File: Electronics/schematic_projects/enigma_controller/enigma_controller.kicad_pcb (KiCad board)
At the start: 6 copper layers, 142.6 x 120.8 mm, 89 parts, among them IC1 TPD8S300ARUKR, IC10 MCP23017-E_SO, IC11 RT9742SNGV, IC13 ESD224DQAR, IC14 ESD224DQAR, IC2 ESD321DYAR, IC3 ESD321DYAR, IC4 ESD321DYAR, IC5 ESD321DYAR, IC6 ESD321DYAR, IC7 ESD321DYAR, IC8 AP22653W6-7, IC9 MCP23017-E_SO, J1 Conn_02x05_Odd_Even, J10 A70-112-331N126, J11 Conn_02x05_Odd_Even, J12 Conn_01x02, J15 Conn_01x02, J16 Conn_01x02, J17 Conn_01x02, J18 Conn_01x02, J19 Conn_01x02, J2 Conn_02x04_Odd_Even, J20 Conn_01x02, J21 Conn_02x05_Odd_Even, J22 Conn_02x05_Odd_Even, J23 Conn_01x02, J24 Conn_01x02, J25 Conn_01x02, J26 Conn_01x02, J27 Conn_01x02, J3 USB1040-GF-L-B, J4 USB_C_Receptacle_USB2.0_16P, J5 HDMI_A_1.4, J6 Conn_02x05_Odd_Even, J7 Conn_02x07_Odd_Even, J8 USB3_A_Stacked, J9 Conn_02x07_Odd_Even, M1 Fan_4pin

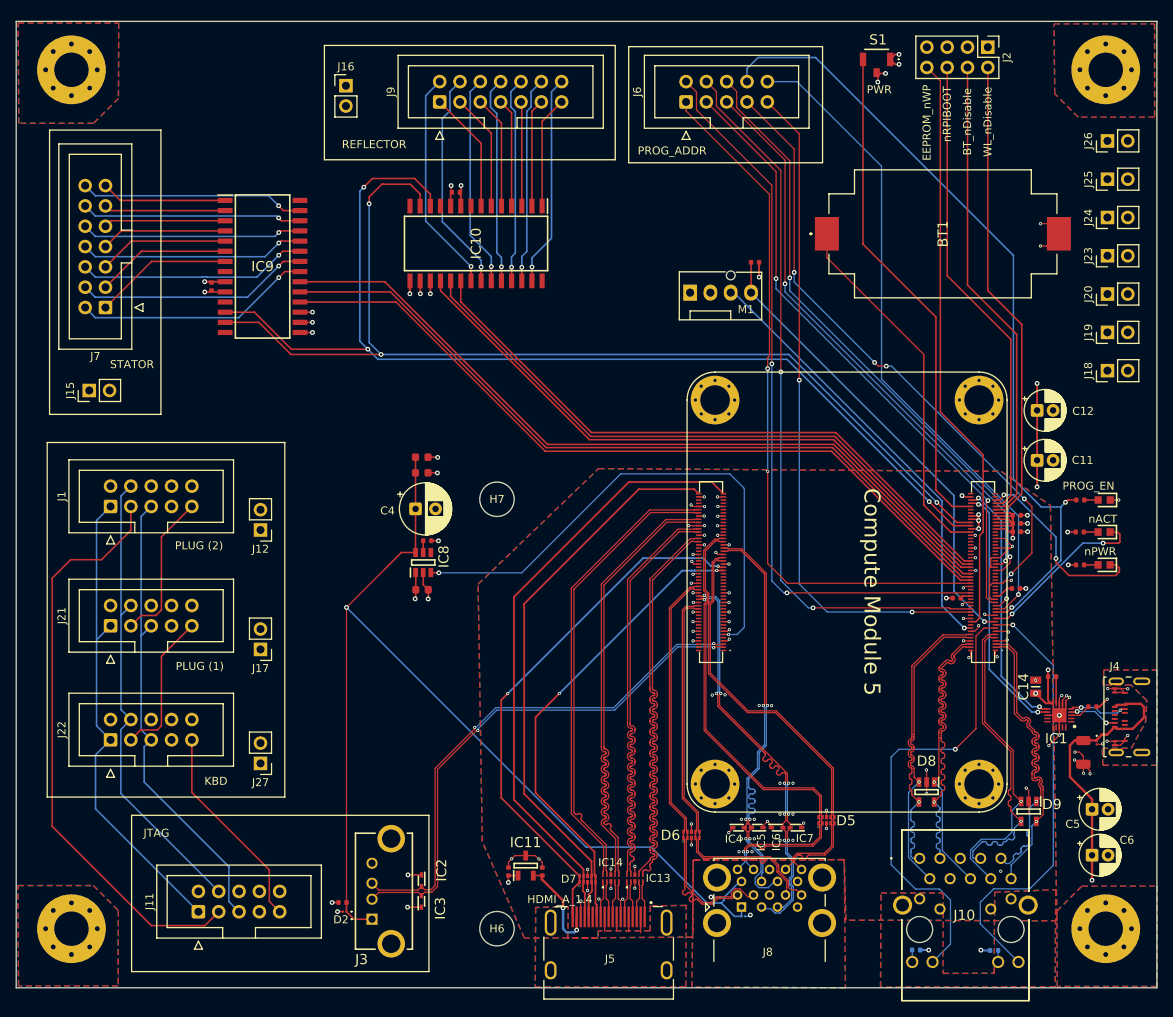
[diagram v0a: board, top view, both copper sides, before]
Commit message: Updated with board-2-board connectors.
Also re-organised components to reduce PCB size.
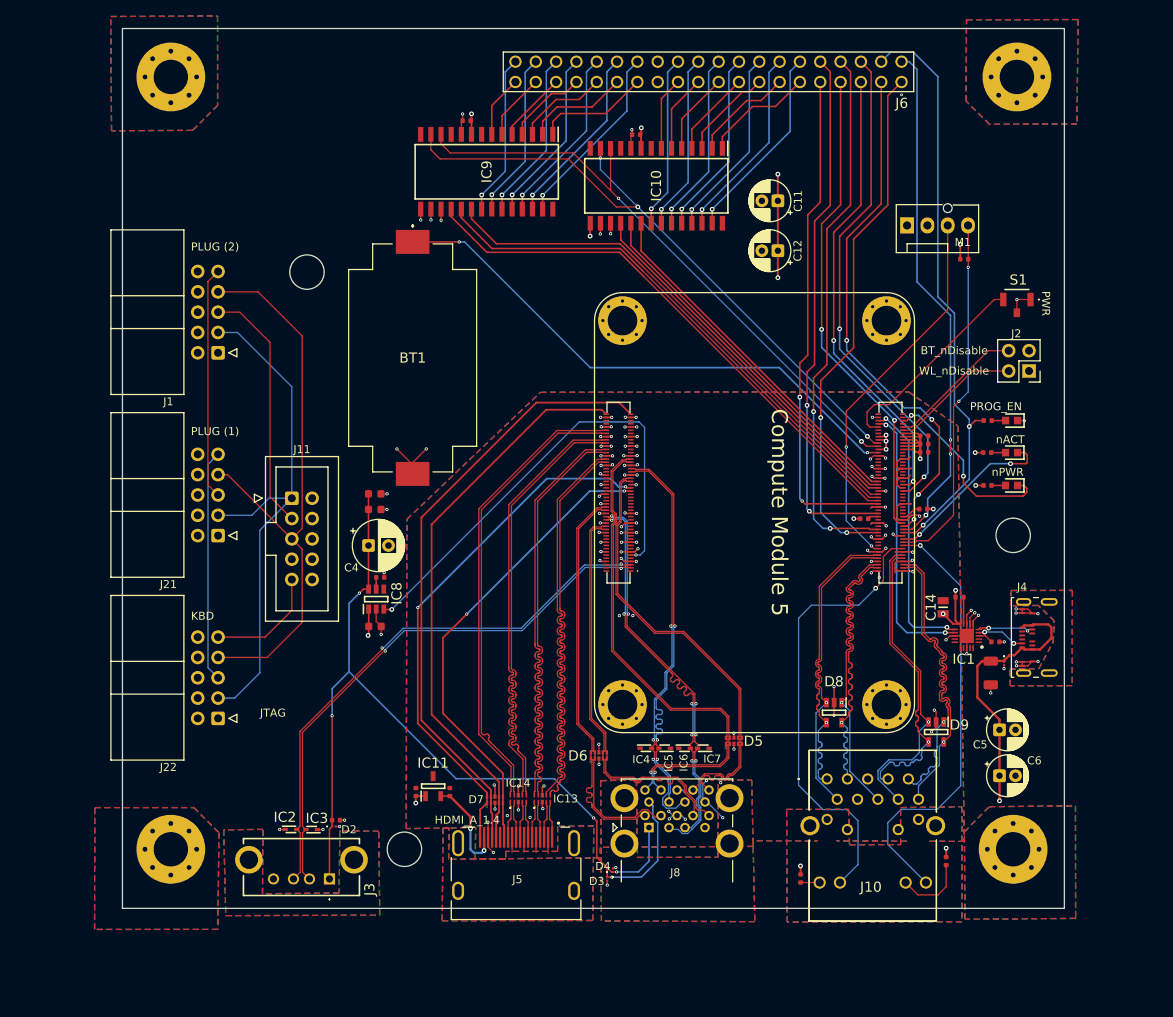
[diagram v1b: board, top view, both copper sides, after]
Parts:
- removed J12, J15, J16, J17, J18, J19, J20, J23, J24, J25, J26, J27: Conn_01x02, Connector_PinHeader_2.54mm:PinHeader_1x02_P2.54mm_Vertical
- removed J7, J9: Conn_02x07_Odd_Even, Connector_IDC:IDC-Header_2x07_P2.54mm_Vertical
- added H8: MountingHole, MountingHole:MountingHole_4.3mm_M4, F.Cu at (193.5, 97.1)
- D3, D4, R3, R4: moved to F.Cu
- J1, J21, J22: footprint Connector_IDC:IDC-Header_2x05_P2.54mm_Vertical -> Connector_IDC:IDC-Header_2x05_P2.54mm_Horizontal
- J2: value Conn_02x04_Odd_Even -> Conn_02x02_Odd_Even; footprint Connector_PinHeader_2.54mm:PinHeader_2x04_P2.54mm_Vertical -> Connector_PinHeader_2.54mm:PinHeader_2x02_P2.54mm_Vertical
- J6: value Conn_02x05_Odd_Even -> ESW-120-33-G-D; footprint Connector_IDC:IDC-Header_2x05_P2.54mm_Vertical -> Enigma_Components:ESW-120-XX-Y-D
- moved BT1 68.1 mm to (118.5, 75.0), turned to 0 degrees
- moved J11 53.0 mm to (103.3, 92.5), turned to 0 degrees
- moved C11 45.9 mm to (164.1, 55.3), turned to 180 degrees
- moved J2 40.8 mm to (195.5, 76.6), turned to 180 degrees
- moved C12 38.1 mm to (164.1, 61.6), turned to 180 degrees
- moved C20 38.0 mm to (125.2, 45.3), turned to 180 degrees
- moved H7 37.0 mm to (105.2, 64.2)
- moved S1 34.8 mm to (194.0, 67.7)
- moved IC9 30.4 mm to (127.7, 51.7), turned to -90 degrees
- moved M1 28.4 mm to (180.3, 58.4)
- moved J6 27.0 mm to (179.6, 40.5), turned to 0 degrees
- moved R8 26.2 mm to (187.4, 62.6), turned to 0 degrees
- moved C17 23.7 mm to (146.4, 47.0)
- moved IC10 23.7 mm to (148.9, 53.4)
- moved J1 23.4 mm to (94.1, 74.3), turned to 180 degrees
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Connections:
- H1 pad 20: /EEPROM_nWP -> unconnected-(H1A-EEPROM_nWP-Pad20)
- H1 pad 93: /nRPIBOOT -> unconnected-(H1A-nRPIBOOT-Pad93)
- J1 pad 1: /TCK -> /VCC_JTAG
- J1 pad 3: /TDO -> /TCK
- J1 pad 4: /VCC_JTAG -> GND
- J1 pad 5: /TMS -> /TDO
- J1 pad 6: unconnected-(J1-Pin_6-Pad6) -> GND
- J1 pad 7: unconnected-(J1-Pin_7-Pad7) -> /TMS
- J1 pad 8: unconnected-(J1-Pin_8-Pad8) -> GND
- J21 pad 1: /TCK -> /VCC_JTAG
- J21 pad 3: /TDX2 -> /TCK
- J21 pad 4: /VCC_JTAG -> GND
- J21 pad 5: /TMS -> /TDX2
- J21 pad 6: unconnected-(J21-Pin_6-Pad6) -> GND
- J21 pad 7: unconnected-(J21-Pin_7-Pad7) -> /TMS
- J21 pad 8: unconnected-(J21-Pin_8-Pad8) -> GND
- J22 pad 1: /TCK -> /VCC_JTAG
- J22 pad 3: /TDX1 -> /TCK
- J22 pad 4: /VCC_JTAG -> GND
- J22 pad 5: /TMS -> /TDX1
- J22 pad 6: unconnected-(J22-Pin_6-Pad6) -> GND
- J22 pad 7: unconnected-(J22-Pin_7-Pad7) -> /TMS
- J22 pad 8: unconnected-(J22-Pin_8-Pad8) -> GND
- J6 pad 1: /MAP_ADDR_1 -> /PROG_nWE_A
- J6 pad 10: /PROG_nWE_B -> /MAP_ADDR_2
- J6 pad 2: /MAP_ADDR_2 -> /PROG_nWE_B
- J6 pad 3: /MAP_ADDR_3 -> /MAP_ADDR_7
- J6 pad 4: /MAP_ADDR_4 -> /PROG_EN
- J6 pad 7: /MAP_ADDR_7 -> /MAP_ADDR_3
- J6 pad 8: /PROG_EN -> /MAP_ADDR_4
- J6 pad 9: /PROG_nWE_A -> /MAP_ADDR_1
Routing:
- net /EEPROM_nWP: track 73.2 -> 0.00 mm
- net /I2C_SCL: track 136.2 -> 76.7 mm, vias 3 -> 2
- net /nRPIBOOT: track 59.1 -> 0.00 mm
- net /VCC_JTAG: track 59.0 -> 0.00 mm
- net /I2C_SDA: track 132.9 -> 82.3 mm
- net /WL_nDisable: track 59.2 -> 16.3 mm
- net /BT_nDisable: track 59.2 -> 17.2 mm
- net /TDO: track 73.0 -> 31.2 mm
- net Net-(H1A-PWR_Button): track 62.8 -> 25.9 mm
- net /EXP2_INT_A: track 79.8 -> 45.0 mm
- net /EXP2_nRST: track 81.8 -> 47.1 mm
- net /EXP2_INT_B: track 80.8 -> 46.1 mm
- net /EXP1_INT_A: track 99.0 -> 66.3 mm
- net /EXP1_INT_B: track 98.6 -> 67.7 mm
- net /EXP1_nRST: track 98.2 -> 69.0 mm
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- added copper zone on In3.Cu, net /VCC_JTAG
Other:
- board size 142.6 x 120.8 mm -> 117.7 x 110 mm
- board text removed: "EEPROM_nWP"
- board text removed: "PROG_ADDR"
- board text removed: "REFLECTOR"
- board text removed: "STATOR"
- board text removed: "nRPIBOOT"

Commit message: Slight re-organisation of USB current limiter.
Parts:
- moved C18 21.6 mm to (114.6, 130.1)
- moved C19 21.6 mm to (114.6, 115.5)
- moved C3 21.6 mm to (114.6, 113.5)
- moved R9 21.6 mm to (115.2, 124.0)
- moved C4 21.6 mm to (113.8, 120.0)
- moved IC8 21.6 mm to (114.8, 126.7)
- moved J4 0.24 mm to (198.1, 109.9)
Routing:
- net /VBUS: track 123.3 -> 95.9 mm, vias 5 -> 2
- net /enigma_controller_HS/VBUS_EN: track 59.9 -> 51.2 mm
- net /JTAG_USB_N: track 68.8 -> 70.7 mm
- net /JTAG_USB_P: track 69.3 -> 70.8 mm

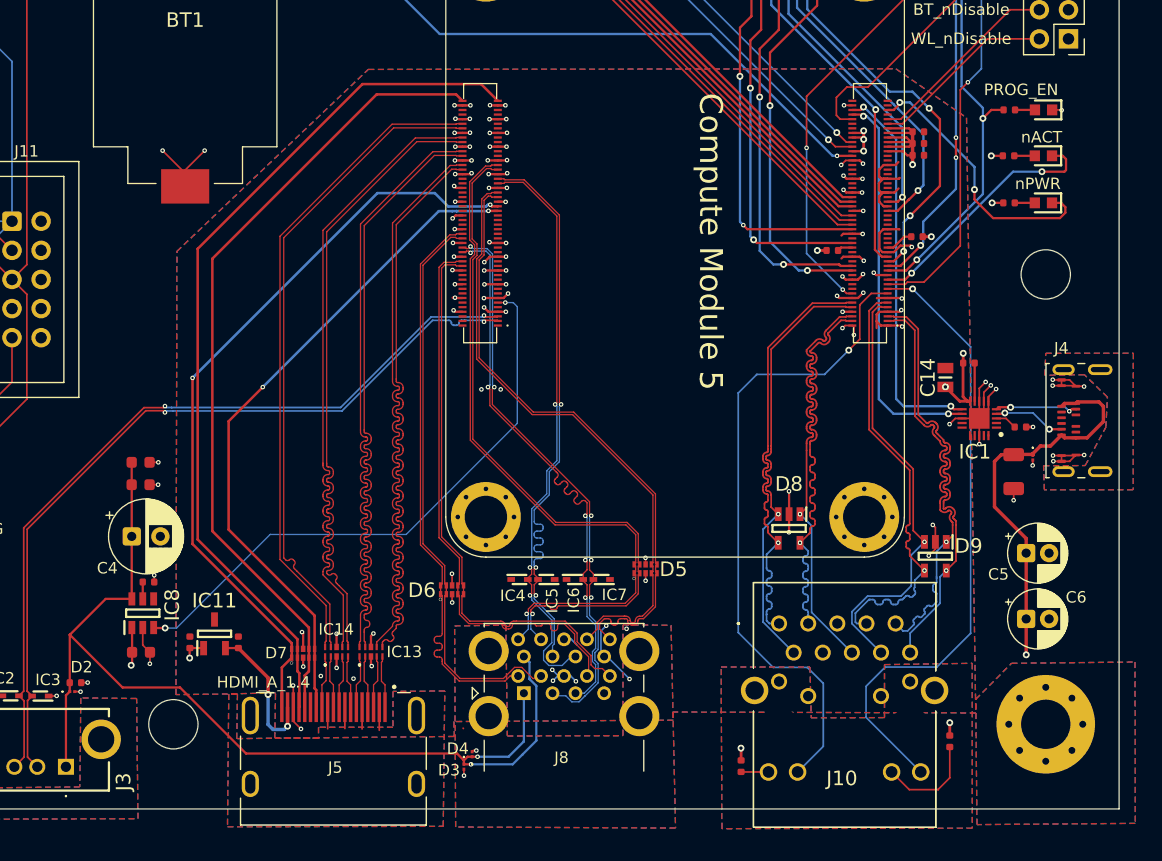
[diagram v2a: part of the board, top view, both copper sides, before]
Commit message: Removed GND flooding. Fixed GND vias.
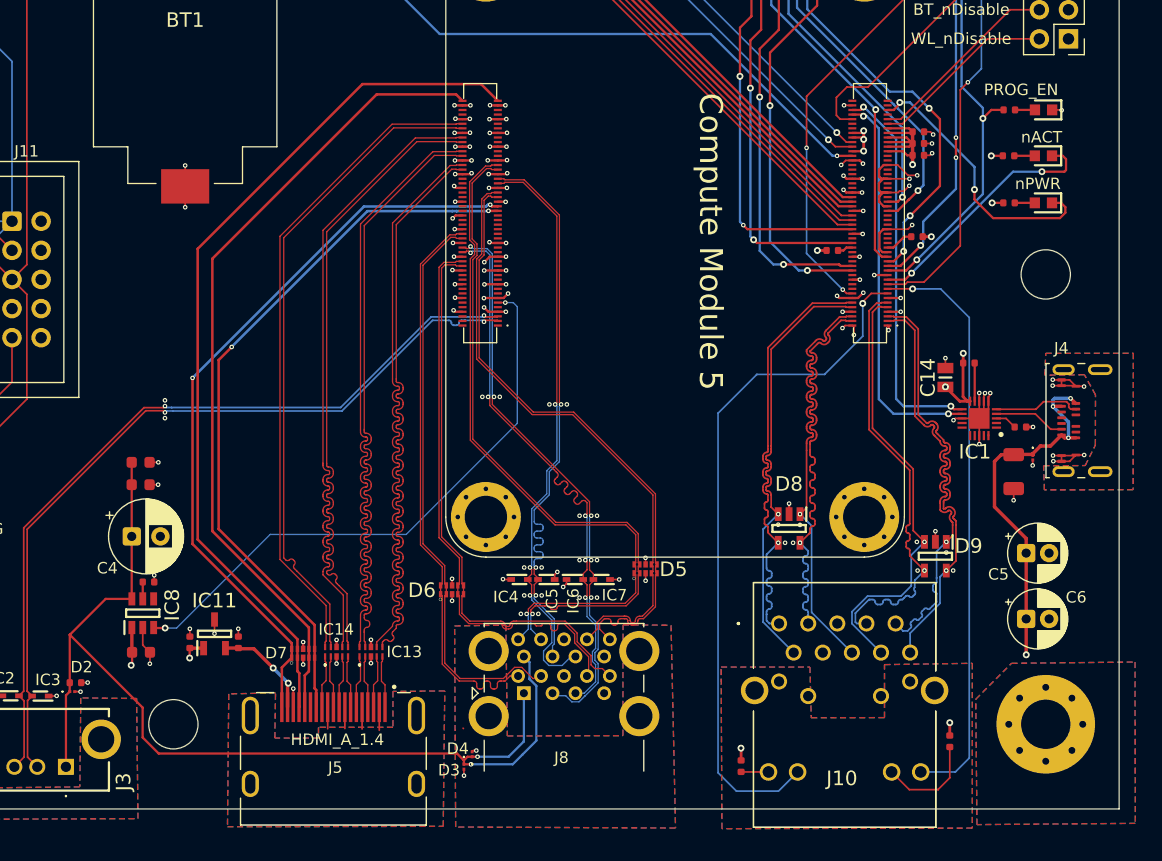
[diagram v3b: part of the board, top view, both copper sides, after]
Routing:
- net GND: track 175.4 -> 158.2 mm, vias 131 -> 157
- net /enigma_controller_HS/HDMI0_CEC: track 59.2 -> 63.6 mm
- net /enigma_controller_HS/HDMI_5V: track 12.7 -> 9.08 mm
- net /ETH_LED_nSpeed: track 54.8 -> 51.3 mm
- net /ETH_LED_nAct: track 57.2 -> 60.5 mm
- net /VBUS: track 95.9 -> 97.4 mm
- net +5V: track 56.4 -> 55.0 mm, vias 4 -> 7
- net /enigma_controller_HS/HDMI0_HOT_PLUG: track 66.6 -> 65.6 mm
- net /C_CC2: track 7.26 -> 7.67 mm, vias 2 -> 0
- net /C_CC1: track 6.30 -> 6.23 mm, vias 2 -> 0
- removed copper zone on B.Cu, net GND
- removed copper zone on F.Cu, net GND
